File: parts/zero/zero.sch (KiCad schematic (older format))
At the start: 12 parts, among them J1 Conn_02x02_Odd_Even, J2 Conn_02x04_Odd_Even, J3 Conn_01x02, K1 HK19F

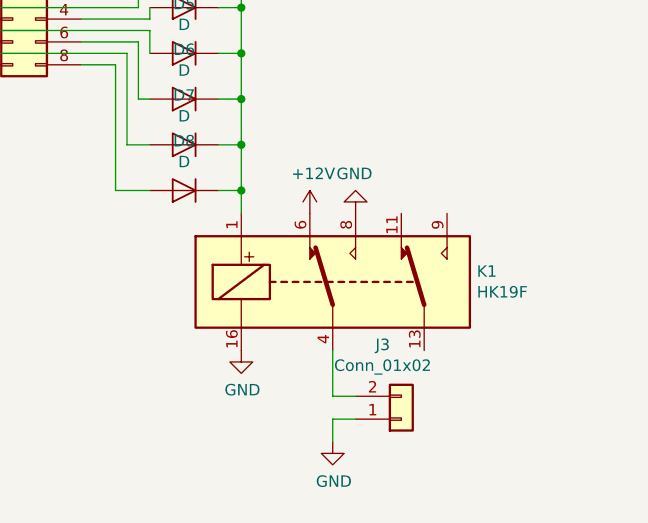
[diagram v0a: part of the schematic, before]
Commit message: Add flyback diode to zero.
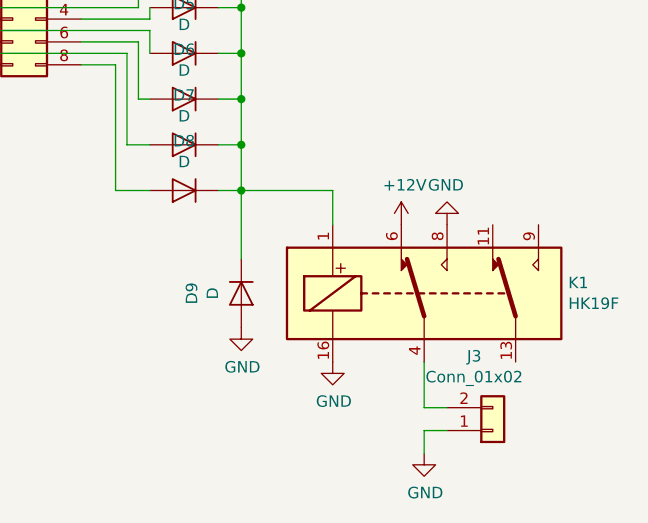
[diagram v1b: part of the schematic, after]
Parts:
- added D9: D, Diodes_SMD:D_2114, symbol Device:D
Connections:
- net GND: now also D9.2 (A)
- net at D1.1 (K), D2.1 (K), D3.1 (K)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: now also D9.1 (K)
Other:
- moved on the sheet: J3, K1
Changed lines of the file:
@@
 L hk19f:HK19F K1
 U 1 1 5C26B097
-P 2500 3050
-F 0 "K1" H 3330 3096 50  0000 L CNN
-F 1 "HK19F" H 3330 3005 50  0000 L CNN
-F 2 "hk19f:Relay_DPDT_HK19F" H 3250 3100 50  0001 C CNN
-F 3 "" H 2500 3050 50  0001 C CNN
-	1    2500 3050
+P 2900 3100
+F 0 "K1" H 3730 3146 50  0000 L CNN
+F 1 "HK19F" H 3730 3055 50  0000 L CNN
+F 2 "hk19f:Relay_DPDT_HK19F" H 3650 3150 50  0001 C CNN
+F 3 "" H 2900 3100 50  0001 C CNN
+	1    2900 3100
 	1    0    0    -1
 $EndComp
-Wire Wire Line
-	2300 2750 2300 2650
 Wire Wire Line
 	2300 1250 2200 1250
 Wire Wire Line
 	2200 2650 2300 2650
-Connection ~ 2300 2650
 Wire Wire Line
 	2300 2650 2300 2450
@@
 L power:GND #PWR07
 U 1 1 5C26F1B9
-P 2300 3350
-F 0 "#PWR07" H 2300 3100 50  0001 C CNN
-F 1 "GND" H 2305 3177 50  0000 C CNN
-F 2 "" H 2300 3350 50  0001 C CNN
-F 3 "" H 2300 3350 50  0001 C CNN
-	1    2300 3350
+P 2700 3400
+F 0 "#PWR07" H 2700 3150 50  0001 C CNN
+F 1 "GND" H 2705 3227 50  0000 C CNN
+F 2 "" H 2700 3400 50  0001 C CNN
+F 3 "" H 2700 3400 50  0001 C CNN
+	1    2700 3400
 	1    0    0    -1
 $EndComp
@@
 L power:GND #PWR06
 U 1 1 5C26F853
-P 2800 2750
-F 0 "#PWR06" H 2800 2500 50  0001 C CNN
-F 1 "GND" H 2805 2577 50  0000 C CNN
-F 2 "" H 2800 2750 50  0001 C CNN
-F 3 "" H 2800 2750 50  0001 C CNN
-	1    2800 2750
+P 3200 2800
+F 0 "#PWR06" H 3200 2550 50  0001 C CNN
+F 1 "GND" H 3205 2627 50  0000 C CNN
+F 2 "" H 3200 2800 50  0001 C CNN
+F 3 "" H 3200 2800 50  0001 C CNN
+	1    3200 2800
 	-1   0    0    1
 $EndComp
@@
 L power:+12V #PWR05
 U 1 1 5C26F99D
-P 2600 2750
-F 0 "#PWR05" H 2600 2600 50  0001 C CNN
-F 1 "+12V" H 2615 2923 50  0000 C CNN
-F 2 "" H 2600 2750 50  0001 C CNN
-F 3 "" H 2600 2750 50  0001 C CNN
-	1    2600 2750
+P 3000 2800
+F 0 "#PWR05" H 3000 2650 50  0001 C CNN
+F 1 "+12V" H 3015 2973 50  0000 C CNN
+F 2 "" H 3000 2800 50  0001 C CNN
+F 3 "" H 3000 2800 50  0001 C CNN
+	1    3000 2800
 	1    0    0    -1
 $EndComp
@@
 L Connector_Generic:Conn_01x02 J3
 U 1 1 5C275517
-P 3000 3650
-F 0 "J3" H 2919 3325 50  0000 C CNN
-F 1 "Conn_01x02" H 2919 3416 50  0000 C CNN
-F 2 "Pin_Headers:Pin_Header_Straight_1x02_Pitch2.54mm" H 3000 3650 50  0001 C CNN
-F 3 "~" H 3000 3650 50  0001 C CNN
-	1    3000 3650
+P 3400 3700
+F 0 "J3" H 3319 3375 50  0000 C CNN
+F 1 "Conn_01x02" H 3319 3466 50  0000 C CNN
+F 2 "Pin_Headers:Pin_Header_Straight_1x02_Pitch2.54mm" H 3400 3700 50  0001 C CNN
+F 3 "~" H 3400 3700 50  0001 C CNN
+	1    3400 3700
 	1    0    0    1
 $EndComp
 Wire Wire Line
-	2700 3350 2700 3550
+	3100 3400 3100 3600
 Wire Wire Line
-	2700 3550 2800 3550
+	3100 3600 3200 3600
 $Comp
 L power:GND #PWR08
 U 1 1 5C27818A
-P 2700 3750
-F 0 "#PWR08" H 2700 3500 50  0001 C CNN
-F 1 "GND" H 2705 3577 50  0000 C CNN
-F 2 "" H 2700 3750 50  0001 C CNN
-F 3 "" H 2700 3750 50  0001 C CNN
-	1    2700 3750
+P 3100 3800
+F 0 "#PWR08" H 3100 3550 50  0001 C CNN
+F 1 "GND" H 3105 3627 50  0000 C CNN
+F 2 "" H 3100 3800 50  0001 C CNN
+F 3 "" H 3100 3800 50  0001 C CNN
+	1    3100 3800
 	1    0    0    -1
 $EndComp
 Wire Wire Line
-	2800 3650 2700 3650
+	3200 3700 3100 3700
 Wire Wire Line
-	2700 3650 2700 3750
+	3100 3700 3100 3800
+Wire Wire Line
+	2700 2800 2700 2650
+Wire Wire Line
+	2700 2650 2300 2650
+Connection ~ 2300 2650
+$Comp
+L Device:D D9
+U 1 1 5C29F29B
+P 2300 3100
+F 0 "D9" H 2300 2884 50  0000 C CNN
+F 1 "D" H 2300 2975 50  0000 C CNN
+F 2 "Diodes_SMD:D_2114" H 2300 3100 50  0001 C CNN
+F 3 "~" H 2300 3100 50  0001 C CNN
+	1    2300 3100
+	0    1    1    0
+$EndComp
+$Comp
+L power:GND #PWR09
+U 1 1 5C29F30E
+P 2300 3250
+F 0 "#PWR09" H 2300 3000 50  0001 C CNN
+F 1 "GND" H 2305 3077 50  0000 C CNN
+F 2 "" H 2300 3250 50  0001 C CNN
+F 3 "" H 2300 3250 50  0001 C CNN
+	1    2300 3250
+	1    0    0    -1
+$EndComp
+Wire Wire Line
+	2300 2950 2300 2650
 $EndSCHEMATC

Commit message: Many things happened at 35C3.
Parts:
- removed J3: Conn_01x02, Pin_Headers:Pin_Header_Straight_1x02_Pitch2.54mm, symbol Connector_Generic:Conn_01x02
- added J3: Conn_02x04_Odd_Even, Pin_Headers:Pin_Header_Straight_2x04_Pitch2.54mm, symbol Connector_Generic:Conn_02x04_Odd_Even
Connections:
- net GND: now also K1.1, J3.1 (Pin_1), J3.3 (Pin_3), J3.5 (Pin_5), J3.7 (Pin_7); no longer K1.16
- net at D1.2 (A), J2.1 (Pin_1): now also J3.8 (Pin_8)
- net at D8.2 (A), J2.8 (Pin_8): now also J3.4 (Pin_4)
- net at D1.1 (K), D2.1 (K), D3.1 (K)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: now also K1.16; no longer K1.1
- net at K1.4: now also J3.6 (Pin_6)
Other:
- moved on the sheet: D1, D2, D3, D4, D5, D6, D7, D8, D9, J2, K1
